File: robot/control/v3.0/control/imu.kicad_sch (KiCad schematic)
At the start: 8 parts, among them J2 BM11B-SRSS-TB, U1 BMI323

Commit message: pinout done
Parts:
- R1, R2: value 100 -> 330
- R3, R4: value 4.7k -> 10k
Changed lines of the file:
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@@
 			)
 		)
-		(property "Value" "100"
+		(property "Value" "330"
 			(at 157.48 35.56 90)
 			(effects
@@
 			)
 		)
-		(property "Value" "100"
+		(property "Value" "330"
 			(at 157.48 33.02 90)
 			(effects
@@
 		(fields_autoplaced yes)
 		(property "Reference" "R3"
-			(at 80.01 37.465 0)
+			(at 80.01 36.8299 0)
 			(effects
 				(font
@@
 			)
 		)
-		(property "Value" "4.7k"
-			(at 80.01 40.005 0)
+		(property "Value" "10k"
+			(at 80.01 39.3699 0)
 			(effects
 				(font
@@
 		(fields_autoplaced yes)
 		(property "Reference" "R4"
-			(at 88.9 37.465 0)
+			(at 88.9 36.8299 0)
 			(effects
 				(font
@@
 			)
 		)
-		(property "Value" "4.7k"
-			(at 88.9 40.005 0)
-			(effects
-				(font
+		(property "Value" "10k"
+			(at 88.9 39.3699 0)
+			(effects
+				(font

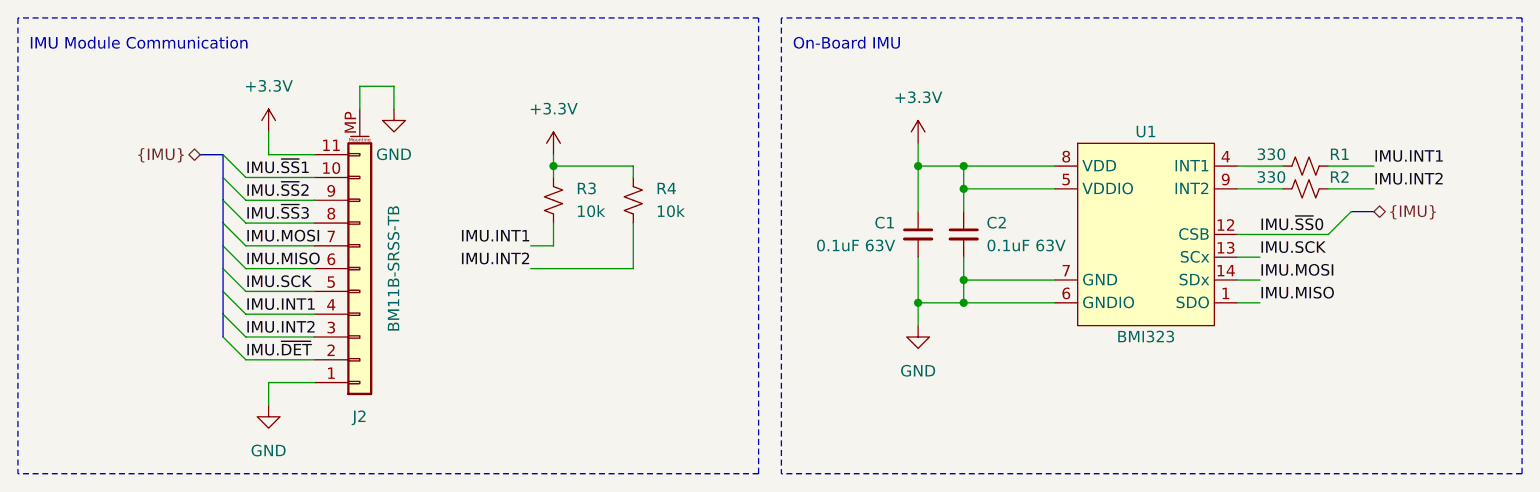
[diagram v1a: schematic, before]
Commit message: control v3 passing ERC
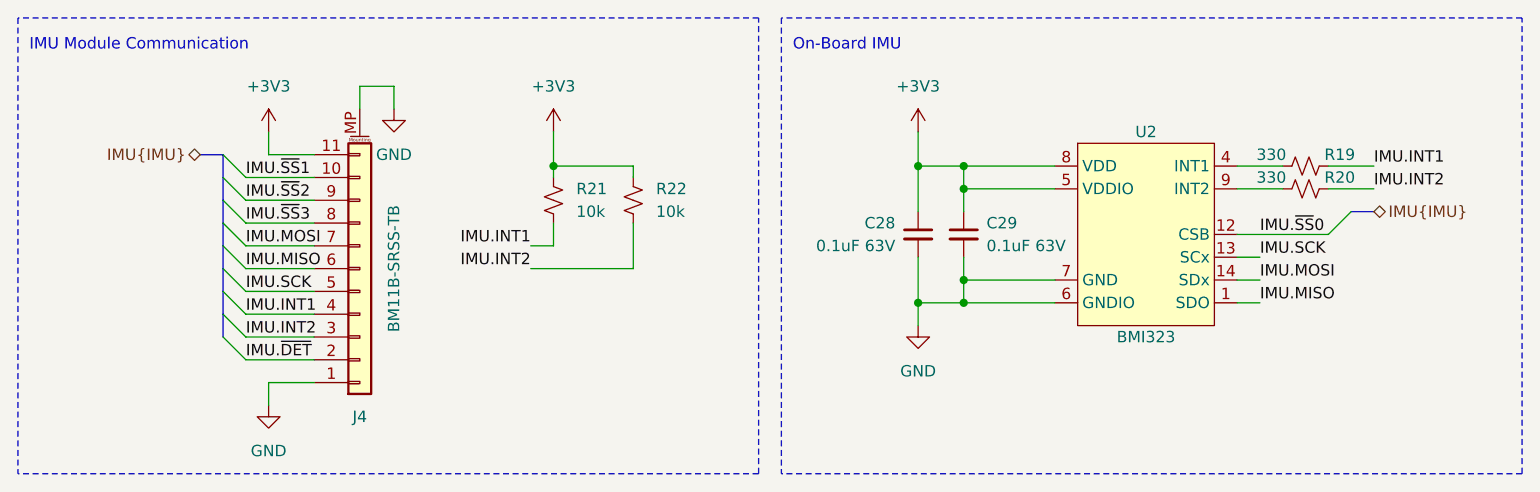
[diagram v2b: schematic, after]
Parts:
- renumbered C1 to C28, C2 to C29, J2 to J4, R1 to R19, R2 to R20, R3 to R21, R4 to R22, U1 to U2
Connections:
- net +3.3V renamed +3V3

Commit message: update boot mode docs, schematic visual fixes, UART default state fixes
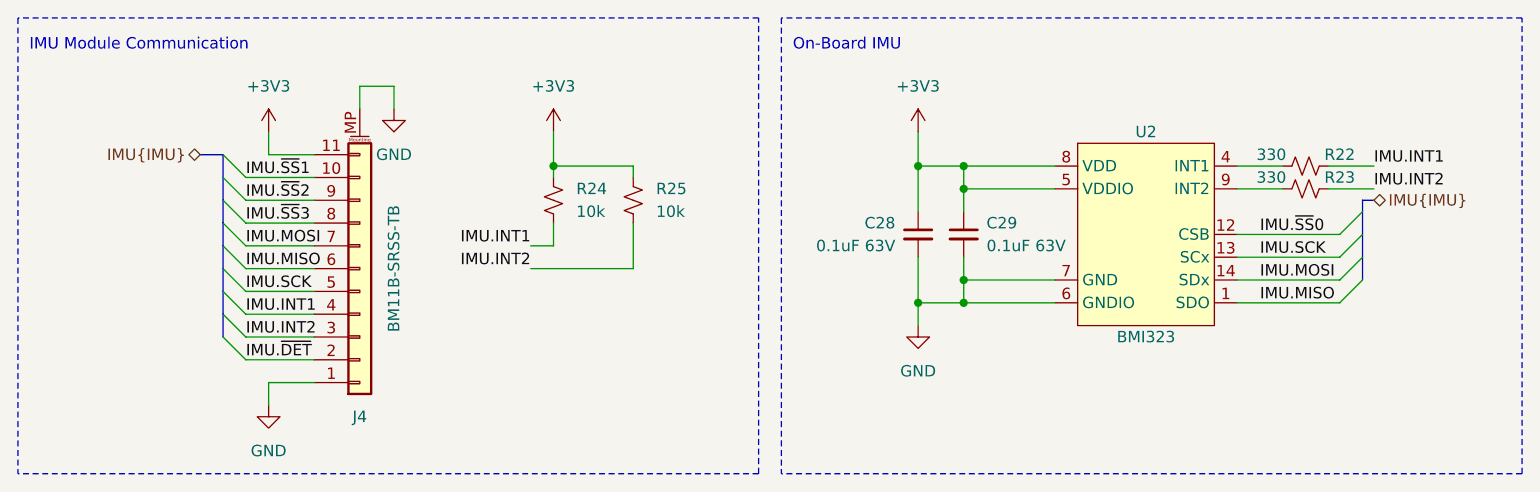
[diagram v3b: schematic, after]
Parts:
- renumbered R19 to R22, R20 to R23, R21 to R24, R22 to R25
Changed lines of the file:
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@@
+	)
+	(bus_entry
+		(at 167.64 41.91)
+		(size -2.54 2.54)
+		(stroke
+			(width 0)
+			(type default)
+		)
 	)
 	(bus_entry
@@
 	)
 	(bus_entry
-		(at 166.37 39.37)
+		(at 167.64 46.99)
+		(size -2.54 2.54)
+		(stroke
+			(width 0)
+			(type default)
+		)
+	)
+	(bus_entry
+		(at 167.64 44.45)
+		(size -2.54 2.54)
+		(stroke
+			(width 0)
+			(type default)
+		)
+	)
+	(bus_entry
+		(at 167.64 39.37)
 		(size -2.54 2.54)
 		(stroke
@@
 	(wire
 		(pts
-			(xy 153.67 44.45) (xy 156.21 44.45)
+			(xy 153.67 44.45) (xy 165.1 44.45)
 		)
 		(stroke
@@
 		)
 	)
+	(bus
+		(pts
+			(xy 167.64 39.37) (xy 167.64 41.91)
+		)
+		(stroke
+			(width 0)
+			(type default)
+		)
+	)
 	(wire
 		(pts
@@
 	(wire
 		(pts
-			(xy 153.67 46.99) (xy 156.21 46.99)
+			(xy 153.67 46.99) (xy 165.1 46.99)
 		)
 		(stroke
@@
 	(wire
 		(pts
-			(xy 153.67 41.91) (xy 163.83 41.91)
+			(xy 153.67 41.91) (xy 165.1 41.91)
 		)
 		(stroke
@@
 		)
 	)
+	(bus
+		(pts
+			(xy 167.64 44.45) (xy 167.64 46.99)
+		)
+		(stroke
+			(width 0)
+			(type default)
+		)
+	)
 	(wire
 		(pts
@@
 	(wire
 		(pts
-			(xy 153.67 49.53) (xy 156.21 49.53)
+			(xy 153.67 49.53) (xy 165.1 49.53)
 		)
 		(stroke
@@
 	(bus
 		(pts
-			(xy 166.37 39.37) (xy 168.91 39.37)
+			(xy 167.64 38.1) (xy 167.64 39.37)
 		)
 		(stroke
@@
 	(bus
 		(pts
+			(xy 167.64 38.1) (xy 168.91 38.1)
+		)
+		(stroke
+			(width 0)
+			(type default)
+		)
+	)
+	(bus
+		(pts
 			(xy 40.64 33.02) (xy 38.1 33.02)
 		)
@@
 		(pts
 			(xy 163.83 36.83) (xy 168.91 36.83)
+		)
+		(stroke
+			(width 0)
+			(type default)
+		)
+	)
+	(bus
+		(pts
+			(xy 167.64 41.91) (xy 167.64 44.45)
 		)
 		(stroke
@@
 		)
 	)
+	(label "IMU.MOSI"
+		(at 156.21 46.99 0)
+		(fields_autoplaced yes)
+		(effects
+			(font
+				(size 1.27 1.27)
+			)
+			(justify left bottom)
+		)
+	)
+	(label "IMU.INT2"
+		(at 168.91 36.83 0)
+		(fields_autoplaced yes)
+		(effects
+			(font
+				(size 1.27 1.27)
+			)
+			(justify left bottom)
+		)
+	)
+	(label "IMU.INT2"
+		(at 74.93 45.72 180)
+		(fields_autoplaced yes)
+		(effects
+			(font
+				(size 1.27 1.27)
+			)
+			(justify right bottom)
+		)
+	)
+	(label "IMU.INT1"
+		(at 43.18 50.8 0)
+		(fields_autoplaced yes)
+		(effects
+			(font
+				(size 1.27 1.27)
+			)
+			(justify left bottom)
+		)
+	)
+	(label "IMU.~{SS}0"
+		(at 156.21 41.91 0)
+		(fields_autoplaced yes)
+		(effects
+			(font
+				(size 1.27 1.27)
+			)
+			(justify left bottom)
+		)
+	)
+	(label "IMU.MISO"
+		(at 156.21 49.53 0)
+		(fields_autoplaced yes)
+		(effects
+			(font
+				(size 1.27 1.27)
+			)
+			(justify left bottom)
+		)
+	)
+	(label "IMU.~{SS}1"
+		(at 43.18 35.56 0)
+		(fields_autoplaced yes)
+		(effects
+			(font
+				(size 1.27 1.27)
+			)
+			(justify left bottom)
+		)
+	)
 	(label "IMU.SCK"
 		(at 156.21 44.45 0)
-		(fields_autoplaced yes)
-		(effects
-			(font
-				(size 1.27 1.27)
-			)
-			(justify left bottom)
-		)
-	)
-	(label "IMU.INT2"
-		(at 168.91 36.83 0)
-		(fields_autoplaced yes)
-		(effects
-			(font
-				(size 1.27 1.27)
-			)
-			(justify left bottom)
-		)
-	)
-	(label "IMU.INT2"
-		(at 74.93 45.72 180)
-		(fields_autoplaced yes)
-		(effects
-			(font
-				(size 1.27 1.27)
-			)
-			(justify right bottom)
-		)
-	)
-	(label "IMU.MOSI"
-		(at 156.21 46.99 0)
-		(fields_autoplaced yes)
-		(effects
-			(font
-				(size 1.27 1.27)
-			)
-			(justify left bottom)
-		)
-	)
-	(label "IMU.INT1"
-		(at 43.18 50.8 0)
-		(fields_autoplaced yes)
-		(effects
-			(font
-				(size 1.27 1.27)
-			)
-			(justify left bottom)
-		)
-	)
-	(label "IMU.MISO"
-		(at 156.21 49.53 0)
-		(fields_autoplaced yes)
-		(effects
-			(font
-				(size 1.27 1.27)
-			)
-			(justify left bottom)
-		)
-	)
-	(label "IMU.~{SS}0"
-		(at 156.21 41.91 0)
-		(fields_autoplaced yes)
-		(effects
-			(font
-				(size 1.27 1.27)
-			)
-			(justify left bottom)
-		)
-	)
-	(label "IMU.~{SS}1"
-		(at 43.18 35.56 0)
 		(fields_autoplaced yes)
 		(effects
@@
 	(hierarchical_label "IMU{IMU}"
 		(shape bidirectional)
-		(at 168.91 39.37 0)
+		(at 168.91 38.1 0)
 		(fields_autoplaced yes)
 		(effects
@@
 		(on_board yes)
 		(dnp no)
-		(property "Reference" "R20"
+		(property "Reference" "R23"
 			(at 165.1 35.56 90)
 			(effects
@@
 			(project "control"
 				(path "/847d0bbe-37dc-4895-9fde-3757dcb8f4e8/69e9d423-5d43-4f6a-9490-973746c2ec4f"
-					(reference "R20")
+					(reference "R23")
 					(unit 1)
 				)
@@
 		(dnp no)
 		(fields_autoplaced yes)
-		(property "Reference" "#PWR077"
+		(property "Reference" "#PWR079"
 			(at 59.69 34.29 0)
 			(effects
@@
 			(project "control"
 				(path "/847d0bbe-37dc-4895-9fde-3757dcb8f4e8/69e9d423-5d43-4f6a-9490-973746c2ec4f"
-					(reference "#PWR077")
+					(reference "#PWR079")
 					(unit 1)
 				)
@@
 		(on_board yes)
 		(dnp no)
-		(property "Reference" "R19"
+		(property "Reference" "R22"
 			(at 165.1 33.02 90)
 			(effects
@@
 			(project "control"
 				(path "/847d0bbe-37dc-4895-9fde-3757dcb8f4e8/69e9d423-5d43-4f6a-9490-973746c2ec4f"
-					(reference "R19")
+					(reference "R22")
 					(unit 1)
 				)
@@
 		(dnp no)
 		(fields_autoplaced yes)
-		(property "Reference" "#PWR082"
+		(property "Reference" "#PWR084"
 			(at 45.72 67.31 0)
 			(effects
@@
 			(project "control"
 				(path "/847d0bbe-37dc-4895-9fde-3757dcb8f4e8/69e9d423-5d43-4f6a-9490-973746c2ec4f"
-					(reference "#PWR082")
+					(reference "#PWR084")
 					(unit 1)
 				)
@@
 		(dnp no)
 		(fields_autoplaced yes)
-		(property "Reference" "#PWR079"
+		(property "Reference" "#PWR081"
 			(at 77.47 34.29 0)
 			(effects
@@
 			(project "control"
 				(path "/847d0bbe-37dc-4895-9fde-3757dcb8f4e8/69e9d423-5d43-4f6a-9490-973746c2ec4f"
-					(reference "#PWR079")
+					(reference "#PWR081")
 					(unit 1)
 				)
@@
 		(dnp no)
 		(fields_autoplaced yes)
-		(property "Reference" "R21"
+		(property "Reference" "R24"
 			(at 80.01 36.8299 0)
 			(effects
@@
 			(project "control"
 				(path "/847d0bbe-37dc-4895-9fde-3757dcb8f4e8/69e9d423-5d43-4f6a-9490-973746c2ec4f"
-					(reference "R21")
+					(reference "R24")
 					(unit 1)
 				)
@@
 		(dnp no)
 		(fields_autoplaced yes)
-		(property "Reference" "#PWR078"
+		(property "Reference" "#PWR080"
 			(at 45.72 34.29 0)
 			(effects
@@
 			(project "control"
 				(path "/847d0bbe-37dc-4895-9fde-3757dcb8f4e8/69e9d423-5d43-4f6a-9490-973746c2ec4f"
-					(reference "#PWR078")
+					(reference "#PWR080")
 					(unit 1)
 				)
@@
 		(dnp no)
 		(fields_autoplaced yes)
-		(property "Reference" "#PWR080"
+		(property "Reference" "#PWR082"
 			(at 118.11 34.29 0)
 			(effects
@@
 			(project "control"
 				(path "/847d0bbe-37dc-4895-9fde-3757dcb8f4e8/69e9d423-5d43-4f6a-9490-973746c2ec4f"
-					(reference "#PWR080")
+					(reference "#PWR082")
 					(unit 1)
 				)
@@
 		(dnp no)
 		(fields_autoplaced yes)
-		(property "Reference" "R22"
+		(property "Reference" "R25"
 			(at 88.9 36.8299 0)
 			(effects
@@
 			(project "control"
 				(path "/847d0bbe-37dc-4895-9fde-3757dcb8f4e8/69e9d423-5d43-4f6a-9490-973746c2ec4f"
-					(reference "R22")
+					(reference "R25")
 					(unit 1)
 				)
@@
 		(dnp no)
 		(fields_autoplaced yes)
-		(property "Reference" "#PWR081"
+		(property "Reference" "#PWR083"
 			(at 118.11 58.42 0)
 			(effects
@@
 			(project "control"
 				(path "/847d0bbe-37dc-4895-9fde-3757dcb8f4e8/69e9d423-5d43-4f6a-9490-973746c2ec4f"
-					(reference "#PWR081")
+					(reference "#PWR083")
 					(unit 1)
 				)
